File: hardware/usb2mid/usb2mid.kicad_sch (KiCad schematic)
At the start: 27 parts, among them J1 USB_C_Receptacle_USB2.0_16P, J2 AudioJack3, U1 STM32G0C1KCUx, U2 USBLC6-2SC6, U3 BU33SD5WG-TR

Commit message: minor corrections + gerber
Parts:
- U1: value STM32G0C1KCUx -> STM32G0C1KCU6

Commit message: changed USB-C footprint
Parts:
- J1: footprint Connector_USB:USB_C_Receptacle_HRO_TYPE-C-31-M-12 -> Connector_USB:USB_C_Receptacle_GCT_USB4105-xx-A_16P_TopMnt_Horizontal
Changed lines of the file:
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@@
+	)
+	(symbol
+		(lib_id "Connector:USB_C_Receptacle_USB2.0_16P")
+		(at 50.8 45.72 0)
+		(unit 1)
+		(exclude_from_sim no)
+		(in_bom yes)
+		(on_board yes)
+		(dnp no)
+		(fields_autoplaced yes)
+		(property "Reference" "J1"
+			(at 50.8 22.86 0)
+			(effects
+				(font
+					(size 1.27 1.27)
+				)
+			)
+		)
+		(property "Value" "USB_C_Receptacle_USB2.0_16P"
+			(at 50.8 25.4 0)
+			(effects
+				(font
+					(size 1.27 1.27)
+				)
+			)
+		)
+		(property "Footprint" "Connector_USB:USB_C_Receptacle_GCT_USB4105-xx-A_16P_TopMnt_Horizontal"
+			(at 54.61 45.72 0)
+			(effects
+				(font
+					(size 1.27 1.27)
+				)
+				(hide yes)
+			)
+		)
+		(property "Datasheet" "https://www.usb.org/sites/default/files/documents/usb_type-c.zip"
+			(at 54.61 45.72 0)
+			(effects
+				(font
+					(size 1.27 1.27)
+				)
+				(hide yes)
+			)
+		)
+		(property "Description" ""
+			(at 50.8 45.72 0)
+			(effects
+				(font
+					(size 1.27 1.27)
+				)
+				(hide yes)
+			)
+		)
+		(pin "A6"
+		)
+		(pin "B5"
+		)
+		(pin "S1"
+		)
+		(pin "A9"
+		)
+		(pin "B4"
+		)
+		(pin "A1"
+		)
+		(pin "A5"
+		)
+		(pin "B9"
+		)
+		(pin "B1"
+		)
+		(pin "A7"
+		)
+		(pin "A4"
+		)
+		(pin "A12"
+		)
+		(pin "B8"
+		)
+		(pin "B6"
+		)
+		(pin "A8"
+		)
+		(pin "B12"
+		)
+		(pin "B7"
+		)
+		(instances
+			(project "usb2mid"
+				(path "/5a6b9954-8f7e-4004-b407-589ad717cf92"
+					(reference "J1")
+					(unit 1)
+				)
+			)
+		)
 	)
 	(symbol
@@
 					(unit 1)
 				)
-			)
-		)
-	)
-	(symbol
-		(lib_id "Connector:USB_C_Receptacle_USB2.0_16P")
-		(at 50.8 45.72 0)
-		(unit 1)
-		(exclude_from_sim no)
-		(in_bom yes)
-		(on_board yes)
-		(dnp no)
-		(fields_autoplaced yes)
-		(property "Reference" "J1"
-			(at 50.8 22.86 0)
-			(effects
-				(font
-					(size 1.27 1.27)
-				)
-			)
-		)
-		(property "Value" "USB_C_Receptacle_USB2.0_16P"
-			(at 50.8 25.4 0)
-			(effects
-				(font
-					(size 1.27 1.27)
-				)
-			)
-		)
-		(property "Footprint" "Connector_USB:USB_C_Receptacle_HRO_TYPE-C-31-M-12"
-			(at 54.61 45.72 0)
-			(effects
-				(font
-					(size 1.27 1.27)
-				)
-				(hide yes)
-			)
-		)
-		(property "Datasheet" "https://www.usb.org/sites/default/files/documents/usb_type-c.zip"
-			(at 54.61 45.72 0)
-			(effects
-				(font
-					(size 1.27 1.27)
-				)
-				(hide yes)
-			)
-		)
-		(property "Description" ""
-			(at 50.8 45.72 0)
-			(effects
-				(font
-					(size 1.27 1.27)
-				)
-				(hide yes)
-			)
-		)
-		(pin "A6"
-		)
-		(pin "B5"
-		)
-		(pin "S1"
-		)
-		(pin "A9"
-		)
-		(pin "B4"
-		)
-		(pin "A1"
-		)
-		(pin "A5"
-		)
-		(pin "B9"
-		)
-		(pin "B1"
-		)
-		(pin "A7"
-		)
-		(pin "A4"
-		)
-		(pin "A12"
-		)
-		(pin "B8"
-		)
-		(pin "B6"
-		)
-		(pin "A8"
-		)
-		(pin "B12"
-		)
-		(pin "B7"
-		)
-		(instances
-			(project "usb2mid"
-				(path "/5a6b9954-8f7e-4004-b407-589ad717cf92"
-					(reference "J1")
-					(unit 1)
-				)

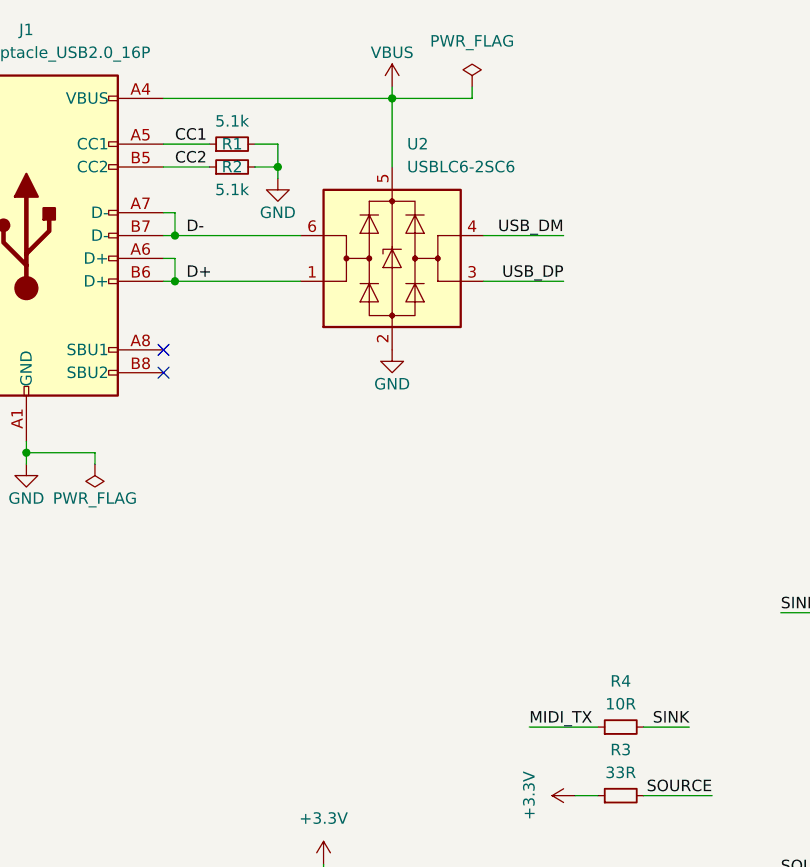
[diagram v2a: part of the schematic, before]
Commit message: oops USB ESD!!
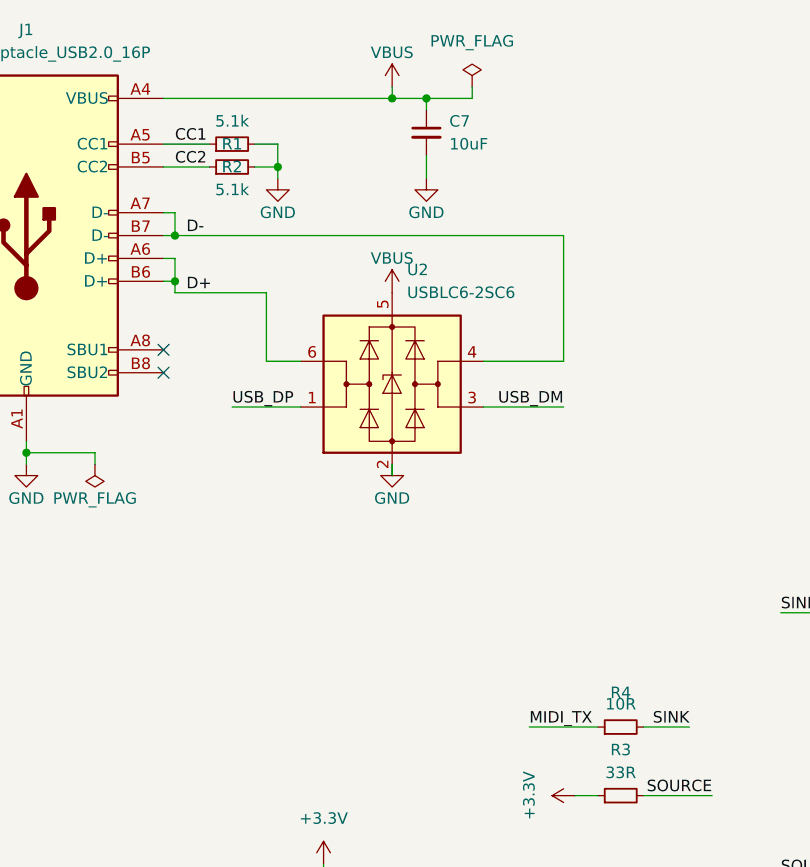
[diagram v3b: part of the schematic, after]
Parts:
- added C7: 10uF, Capacitor_SMD:C_0603_1608Metric, symbol Device:C_Small
- C2: footprint Capacitor_SMD:C_0402_1005Metric -> Capacitor_SMD:C_0603_1608Metric
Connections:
- net D+: now also U2.6 (I/O1); no longer U2.1 (I/O1)
- net D-: now also U2.4 (I/O2); no longer U2.6 (I/O1)
- net GND: now also C7.2
- net USB_DM: now also U2.3 (I/O2); no longer U2.4 (I/O2)
- net USB_DP: now also U2.1 (I/O1); no longer U2.3 (I/O2)
- net VBUS: now also C7.1
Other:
- moved on the sheet: U2
